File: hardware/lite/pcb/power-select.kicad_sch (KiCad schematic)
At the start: 23 parts, among them Q1911 2N7002, Q1912 2N7002, U1901 AP22653W6-7, U1902 TPS259470LRPWR

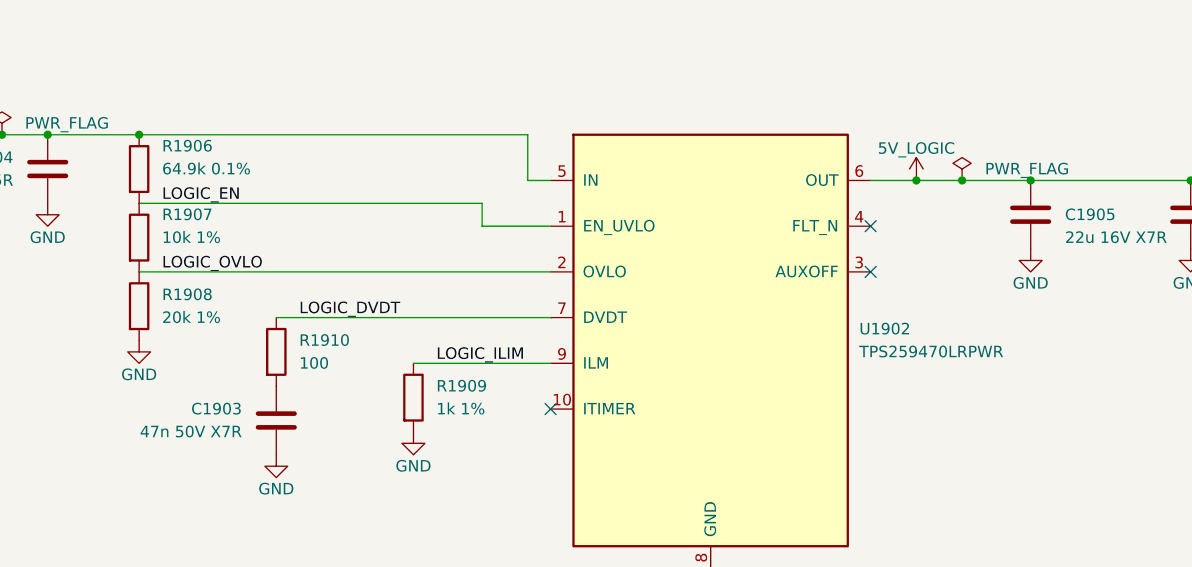
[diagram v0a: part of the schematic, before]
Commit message: feat(hardware): share brick power across ports and add CM5 link
A connected PD supply now runs the logic through its own buck and feeds
one TPS55288 buck-boost stage per port, so the contract is shared as
5-20 V at up to 5 A per port. The hub's VBUS detect becomes an OR gate,
a host-select mux lets a CM5 side board drive the hub over a 24-pin ZIF
link, and a CM5 variant joins Hub and HubPD.

The board is synced to the schematic and its old routing removed; the
new parts wait below the outline for placement.
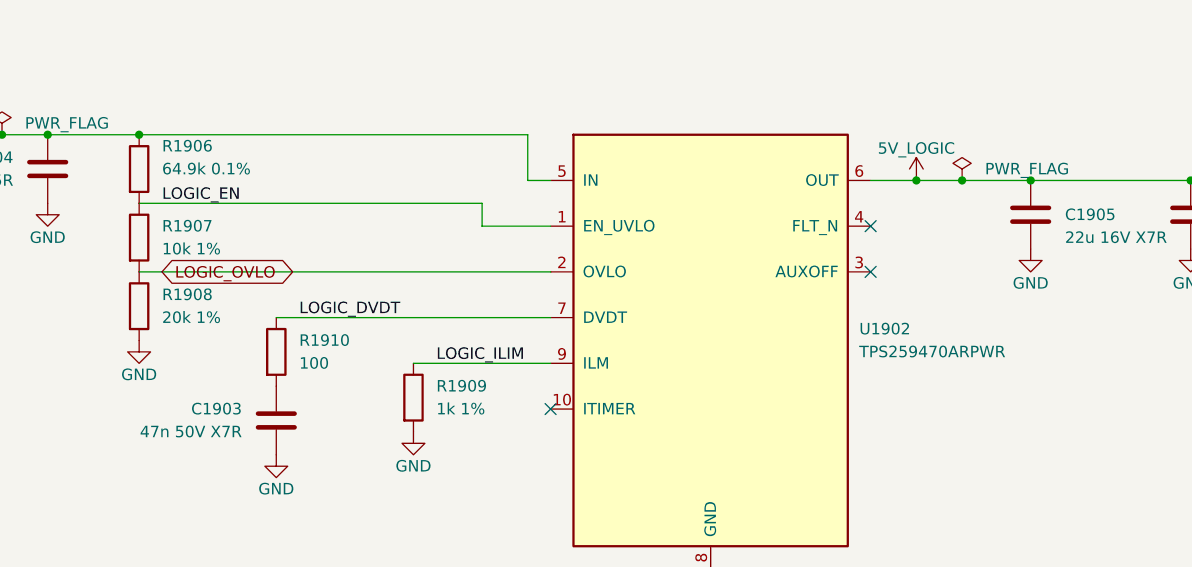
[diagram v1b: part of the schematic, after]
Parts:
- U1902: value TPS259470LRPWR -> TPS259470ARPWR; LCSC C3662793 -> C3662799; MPN TPS259470LRPWR -> TPS259470ARPWR
